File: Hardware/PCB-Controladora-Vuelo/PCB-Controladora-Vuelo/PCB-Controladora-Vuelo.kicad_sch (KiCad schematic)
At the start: 3 parts, among them U1 GY-521, U2 ESP32-DEVKIT-V1, U3 NRF24L01_Breakout

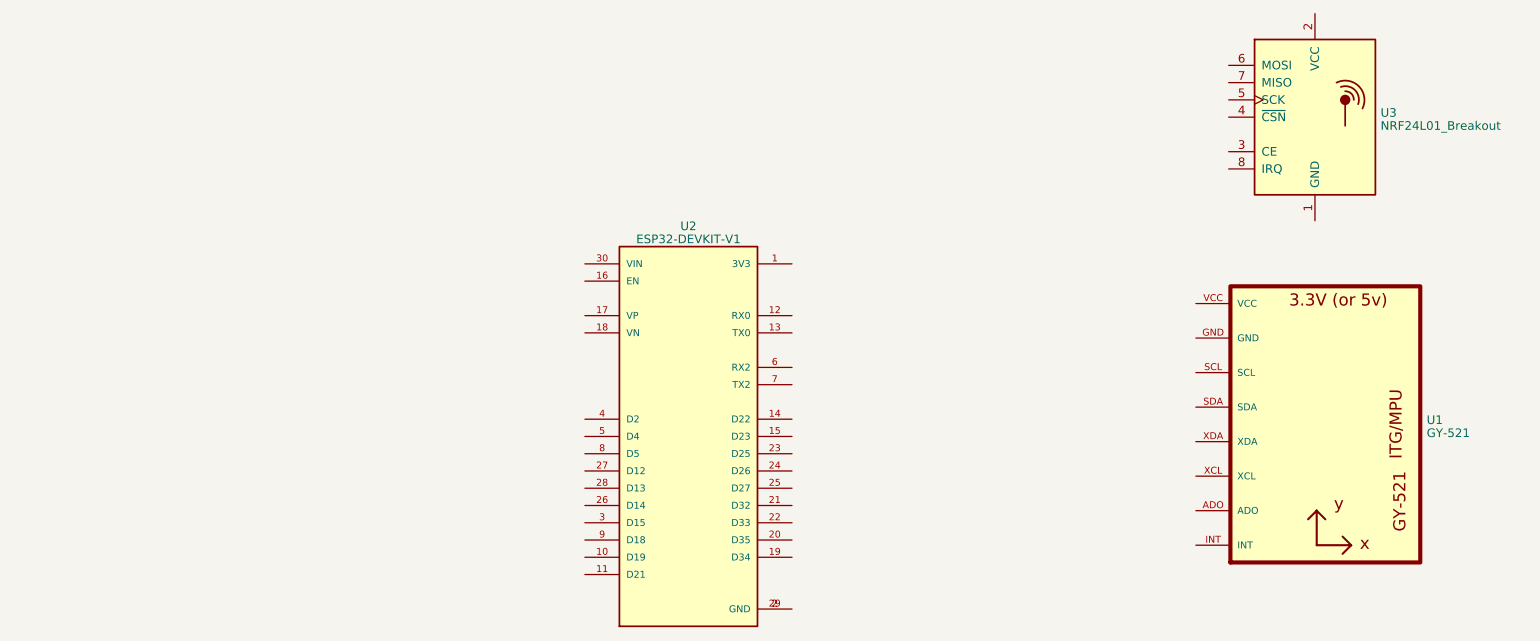
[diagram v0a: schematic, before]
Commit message: Ordene un poco y agregue las librerias de los simbolos y footprints que faltaban
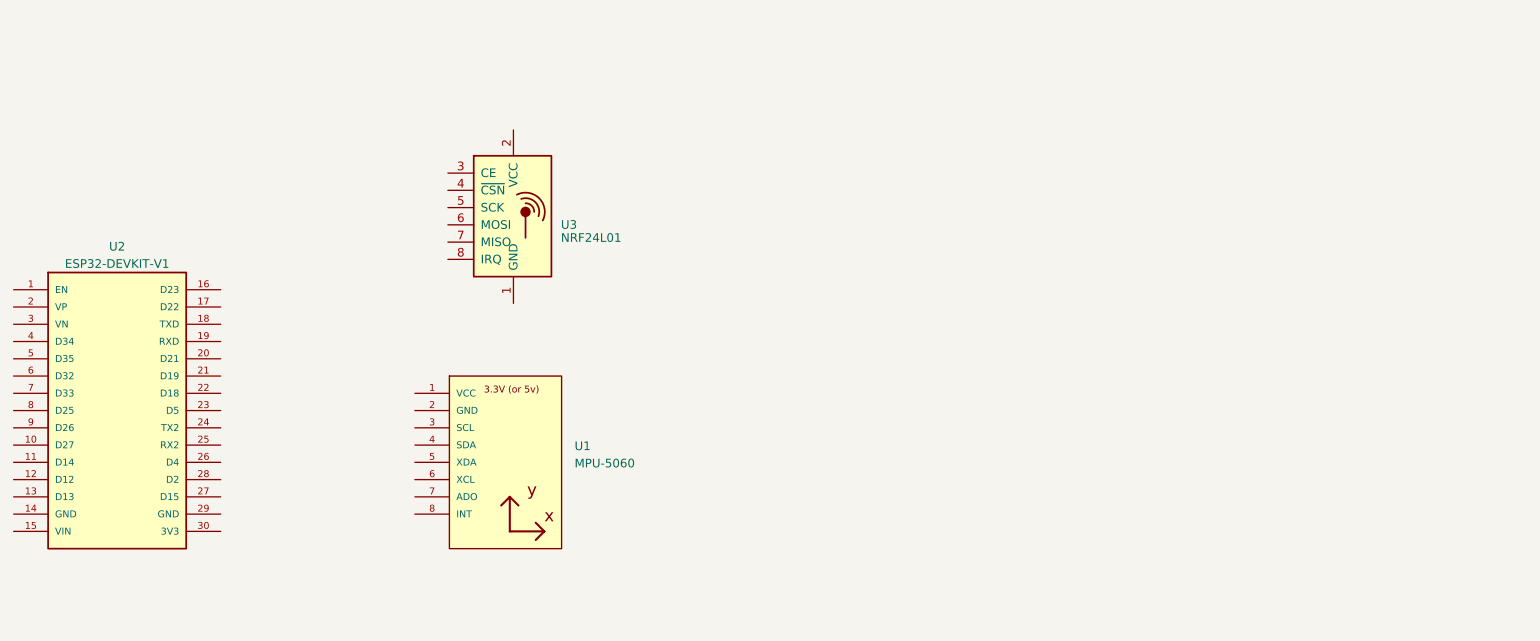
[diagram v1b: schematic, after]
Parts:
- removed U1: GY-521, GY-521, symbol GY-521:GY-521
- removed U2: ESP32-DEVKIT-V1, MODULE_ESP32_DEVKIT_V1, symbol ESP32-DEVKIT-V1:ESP32-DEVKIT-V1
- added U1: MPU-5060, MPU-5060, symbol Librerias:MPU-5060
- added U2: ESP32-DEVKIT-V1, MODULE_ESP32_DEVKIT_V1-30Pines, symbol Librerias:ESP32-DEVKIT-V1-30pines
- U3: value NRF24L01_Breakout -> NRF24L01; footprint RF_Module:nRF24L01_Breakout -> (none)

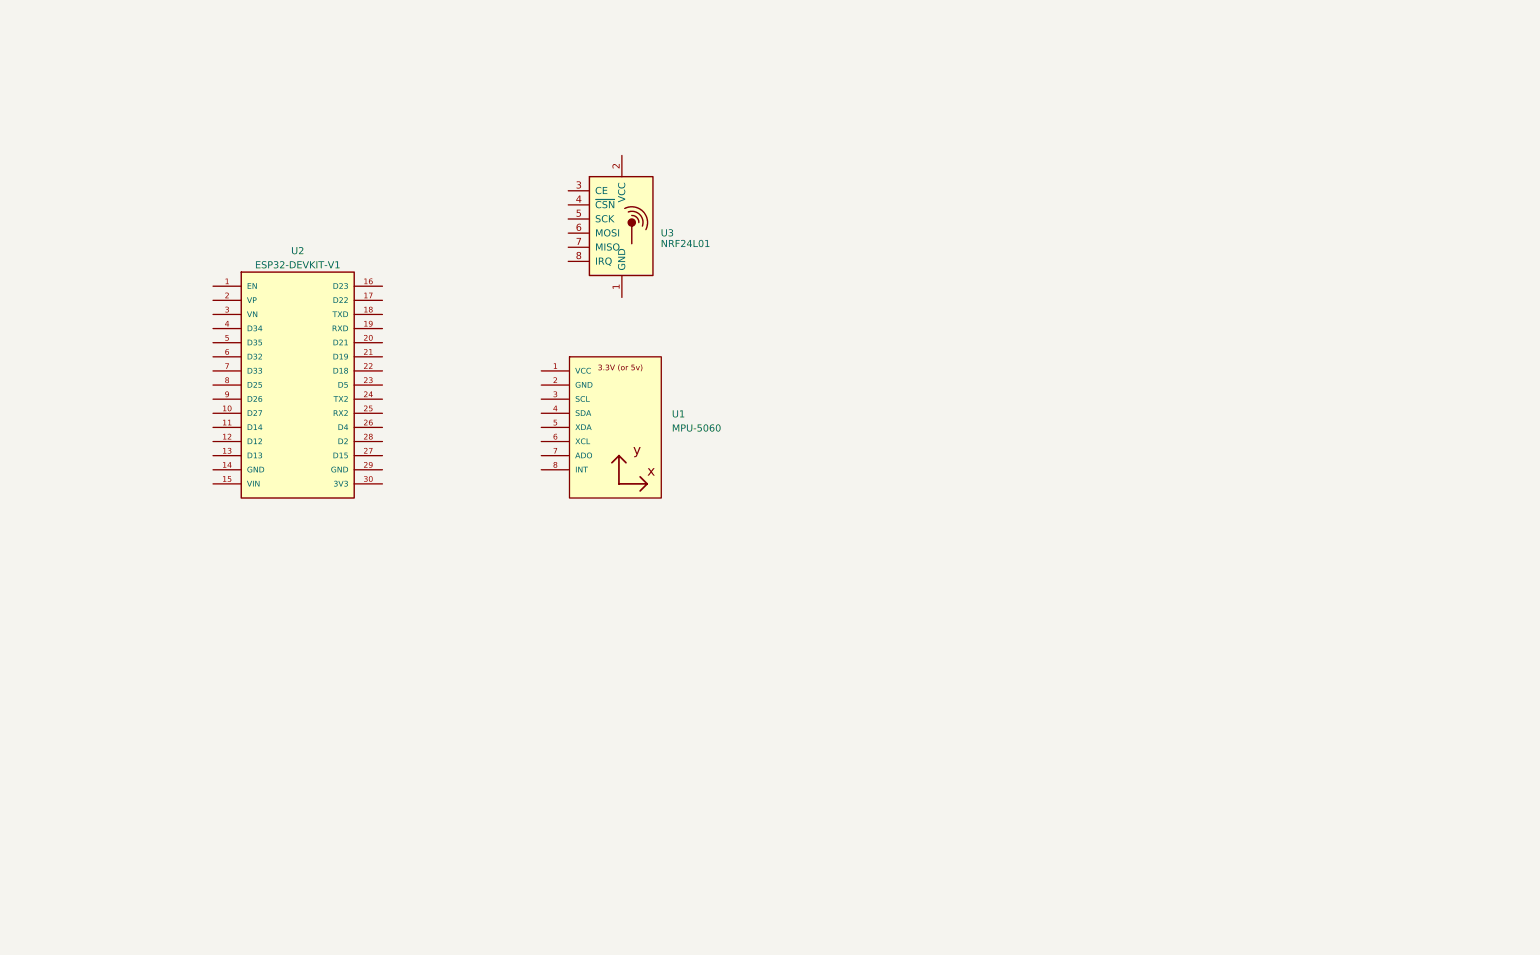
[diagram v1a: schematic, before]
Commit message: cambios en el sch de la Controladora de Vuelo se agrega a la rama los cambios hechos por eze y ademas agregue  la alimentacion y ordene, me quedan las conexiones y hacer el symbolo de  la controladora de motores
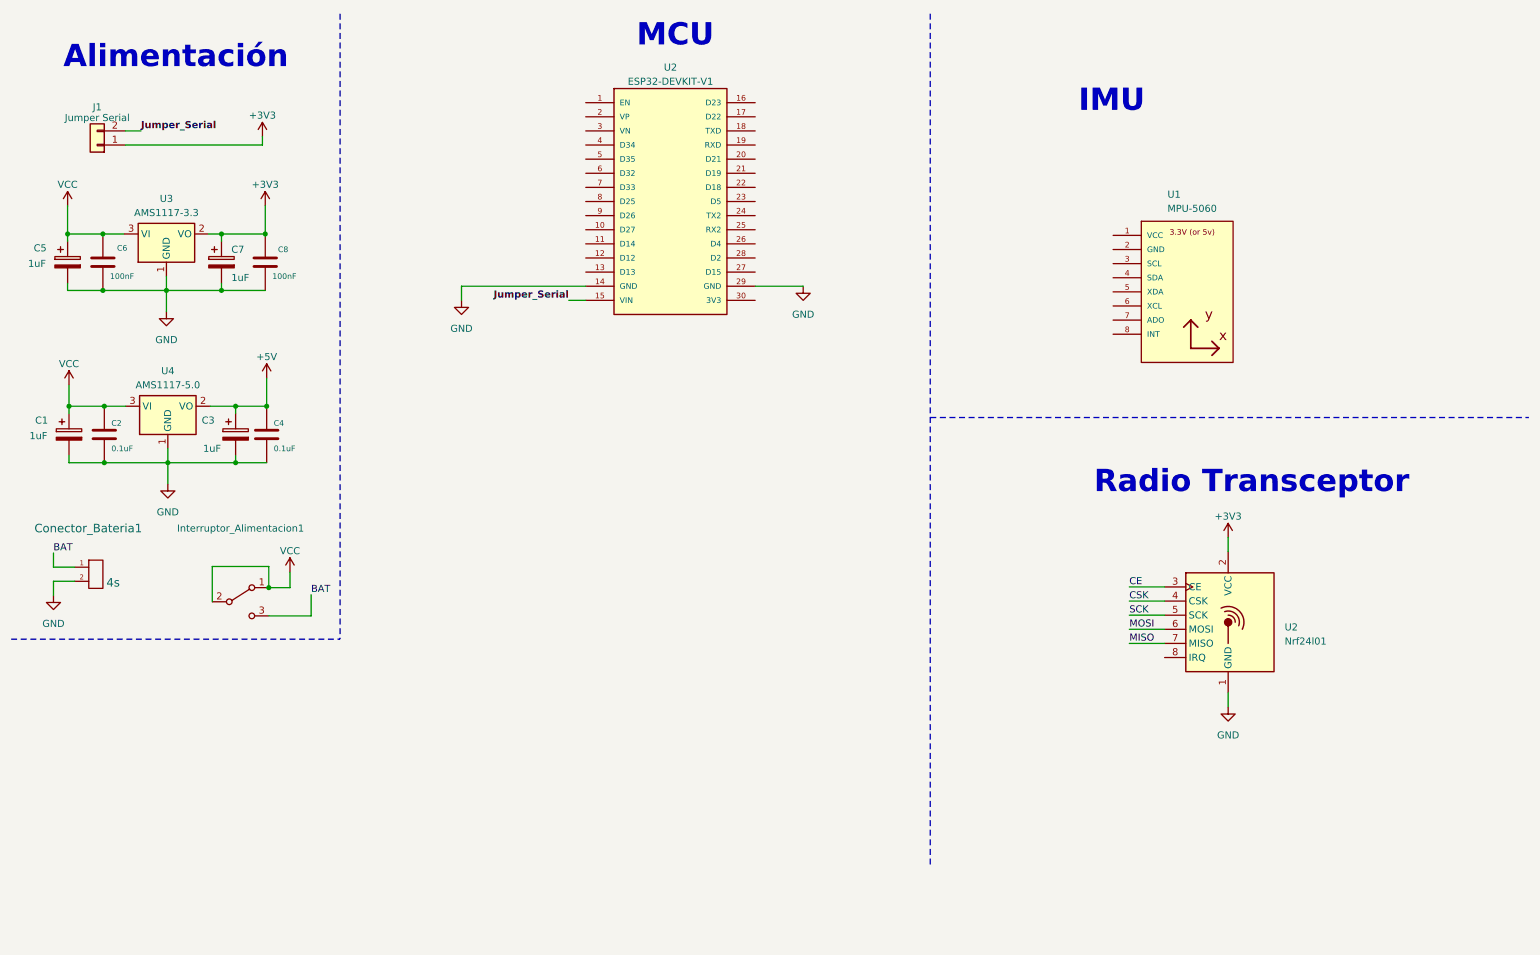
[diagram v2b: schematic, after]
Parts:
- removed U3: NRF24L01, symbol RF:NRF24L01_Breakout
- added C1, C3, C5, C7: 1uF, EESTN5:CAP_ELEC_5x11mm, symbol Device:C_Polarized
- added C2, C4: 0.1uF, EESTN5:CAP_0.1, symbol EESTN5:C
- added C6, C8: 100nF, EESTN5:CAP_0.1, symbol EESTN5:C
- added Conector_Bateria1: 4s, EESTN5:Pin_Header_2, symbol EESTN5:HEADER_2
- added Interruptor_Alimentacion1: SW_SPDT, EESTN5:Pin_Header_3, symbol EESTN5:SW_SPDT
- added J1: Jumper Serial, symbol Connector_Generic:Conn_01x02
- added U2: Nrf24l01, RF_Module:nRF24L01_Breakout, symbol EESTN5:Nrf24l01
- added U3: AMS1117-3.3, Package_TO_SOT_SMD:SOT-223-3_TabPin2, symbol Regulator_Linear:AMS1117-3.3
- added U4: AMS1117-5.0, Package_TO_SOT_SMD:SOT-223-3_TabPin2, symbol Regulator_Linear:AMS1117-5.0
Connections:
- net GND: now reaches U2.14 (GND)
- net GND: now also U2.29 (GND), C1.2, C2.2, C3.2, C4.2, C5.2, C6.2, C7.2, C8.2, Conector_Bateria1.2, U2.1 (GND), U3.1 (GND), U4.1 (GND)
- net Jumper_Serial: now reaches U2.15 (VIN)
- net Jumper_Serial: now also J1.2 (Pin_2)
- new net +3V3: C7.1, C8.1, J1.1 (Pin_1), U2.2 (VCC), U3.2 (VO)
- new net +5V: C3.1, C4.1, U4.2 (VO)
- new net BAT: Conector_Bateria1.1, Interruptor_Alimentacion1.3 (C)
- new net CE: U2.3 (CE)
- new net CSK: U2.4 (CSK)
- new net MISO: U2.7 (MISO)
- new net MOSI: U2.6 (MOSI)
- new net SCK: U2.5 (SCK)
- new net VCC: C1.1, C2.1, C5.1, C6.1, Interruptor_Alimentacion1.1 (A), Interruptor_Alimentacion1.2 (B), U3.3 (VI), U4.3 (VI)
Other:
- note added: "Alimentación"
- note added: "IMU"
- note added: "MCU"
- note added: "Radio Transceptor"
- moved on the sheet: U1, U2

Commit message: Agregue conexiones i2c imu y spi transceptor tambien modifique la alimentacion por vin para el uC
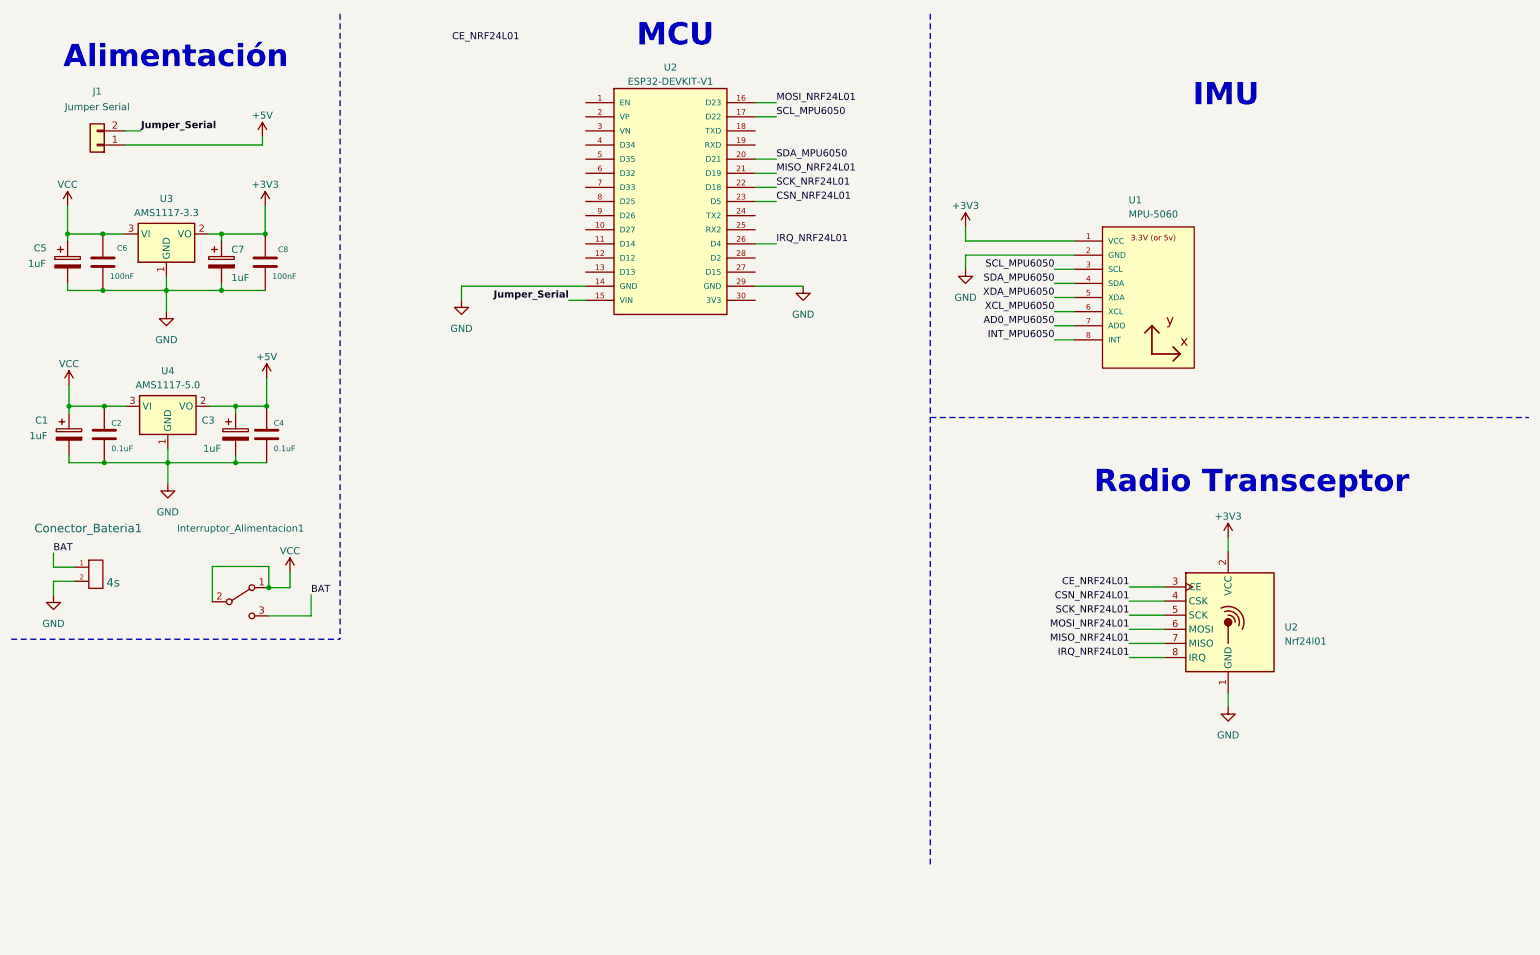
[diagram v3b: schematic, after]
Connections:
- net CSK is gone; now on net CSN_NRF24L01: U2.4 (CSK)
- net MISO is gone; now on net MISO_NRF24L01: U2.7 (MISO)
- net MOSI is gone; now on net MOSI_NRF24L01: U2.6 (MOSI)
- net SCK is gone; now on net SCK_NRF24L01: U2.5 (SCK)
- net +3V3: now also U1.1 (VCC); no longer J1.1 (Pin_1)
- net +5V: now also J1.1 (Pin_1)
- net GND: now also U1.2 (GND)
- net SCL_MPU6050: now reaches U1.3 (SCL)
- net SCL_MPU6050: now also U2.17 (D22)
- net SDA_MPU6050: now reaches U1.4 (SDA)
- net SDA_MPU6050: now also U2.20 (D21)
- net XDA_MPU6050: now reaches U1.5 (XDA)
- net XCL_MPU6050: now reaches U1.6 (XCL)
- net AD0_MPU6050: now reaches U1.7 (ADO)
- net INT_MPU6050: now reaches U1.8 (INT)
- net MOSI_NRF24L01: now reaches U2.16 (D23)
- net MISO_NRF24L01: now reaches U2.21 (D19)
- net SCK_NRF24L01: now reaches U2.22 (D18)
- net CSN_NRF24L01: now reaches U2.23 (D5)
- net IRQ_NRF24L01: now reaches U2.26 (D4)
- net IRQ_NRF24L01: now also U2.8 (IRQ)
- net CE renamed CE_NRF24L01
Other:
- moved on the sheet: U1

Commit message: Avances en el PCB de la controladora de vuelo
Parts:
- removed C1, C3: 1uF, EESTN5:CAP_ELEC_5x11mm, symbol Device:C_Polarized
- removed C2, C4: 0.1uF, EESTN5:CAP_0.1, symbol EESTN5:C
- removed Conector_Bateria1: 4s, EESTN5:Pin_Header_2, symbol EESTN5:HEADER_2
- removed Interruptor_Alimentacion1: SW_SPDT, EESTN5:Pin_Header_3, symbol EESTN5:SW_SPDT
- removed U4: AMS1117-5.0, Package_TO_SOT_SMD:SOT-223-3_TabPin2, symbol Regulator_Linear:AMS1117-5.0
- added H1, H2, H3, H4: Mounting_Hole, EESTN5:hole_3mm, symbol EESTN5:Mounting_Hole
- added J2: CONN, Footprints:JST10mm, symbol Librerias:JST-1mm
- C5, C7: footprint EESTN5:CAP_ELEC_5x11mm -> Capacitor_SMD:C_1206_3216Metric
- C6, C8: footprint EESTN5:CAP_0.1 -> Capacitor_SMD:C_1206_3216Metric
- J1: footprint (none) -> Connector_PinHeader_1.27mm:PinHeader_1x02_P1.27mm_Vertical
- U1: footprint MPU-5060 -> Footprints:MPU-6050
- U2: footprint MODULE_ESP32_DEVKIT_V1-30Pines -> Footprints:ESP32-DEVKIT-V1-30Pines
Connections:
- net VCC is gone; now on net +5V: C5.1, C6.1, U3.3 (VI)
- net +5V: now also J2.6
- net GND: now also J2.2, J2.5
- net S2_MOTOR: now reaches U2.10 (D27)
- net S2_MOTOR: now also J2.8
- net S3_MOTOR: now reaches U2.11 (D14)
- net S3_MOTOR: now also J2.9
- net S4_MOTOR: now reaches U2.12 (D12)
- net S4_MOTOR: now also J2.10
- net S1_MOTOR: now reaches U2.9 (D26)
- net S1_MOTOR: now also J2.7
- new net NC: J2.1, J2.3, J2.4, J2.S1 (SHIELD), J2.S2 (SHIELD)
